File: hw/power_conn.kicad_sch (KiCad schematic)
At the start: 2 parts, among them J4 Conn_01x02, J5 Conn_01x02

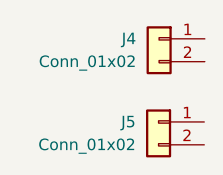
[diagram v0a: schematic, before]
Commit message: began with lcsc and footprints
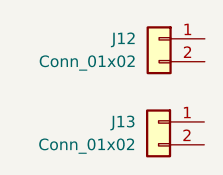
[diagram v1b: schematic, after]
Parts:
- renumbered J4 to J12, J5 to J13
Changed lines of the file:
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@@
 		(in_pos_files yes)
 		(dnp no)
-		(property "Reference" "J4"
+		(property "Reference" "J12"
 			(at 114.3 99.0599 0)
 			(show_name no)
@@
 			(project "atlas-electronics"
 				(path "/915bc1ff-7be5-4368-a2db-c4889af73afd/31111bce-c3cf-4571-96fd-1e6d0b264e78"
-					(reference "J4")
+					(reference "J12")
 					(unit 1)
 				)
@@
 		(in_pos_files yes)
 		(dnp no)
-		(property "Reference" "J5"
+		(property "Reference" "J13"
 			(at 114.24 108.2969 0)
 			(show_name no)
@@
 			(project "atlas-electronics"
 				(path "/915bc1ff-7be5-4368-a2db-c4889af73afd/31111bce-c3cf-4571-96fd-1e6d0b264e78"
-					(reference "J5")
+					(reference "J13")
 					(unit 1)
 				)
